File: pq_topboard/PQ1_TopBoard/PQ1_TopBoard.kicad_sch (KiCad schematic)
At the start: 11 parts, among them IC3 TCN75AVUA713, J2 Conn_01x11_MountingPin

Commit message: Functional revision and finishing touches part II
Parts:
- removed D8: SLCD-61N8, SOD-123_L2.8-W1.8-LS3.7-RD, symbol Top_board-altium-import:1_SLCD-61N8
- removed GA6, GA7, GA8: 5k, R0805, symbol Top_board-altium-import:1_5k
- removed R11, R12, VA6, VA7, VA8: 5k, R0805, symbol Top_board-altium-import:0_5k
- added Annotation1: Silkscreen_Annotation, symbols-nsl:IEEE_logo, symbol symbols-nsl:Silkscreen_Annotation
- added Annotation2: Silkscreen_Annotation, symbols-nsl:GRSS, symbol symbols-nsl:Silkscreen_Annotation
- added Annotation3: Silkscreen_Annotation, symbols-nsl:NSL_long, symbol symbols-nsl:Silkscreen_Annotation
- added Annotation4: Silkscreen_Annotation, symbols-nsl:Telecos, symbol symbols-nsl:Silkscreen_Annotation
- added Annotation5: Silkscreen_Annotation, symbols-nsl:UPC_positiu, symbol symbols-nsl:Silkscreen_Annotation
- added C1: 1 uF, Capacitor_SMD:C_0603_1608Metric, symbol Device:C
- added D1: SLCD-61N8, passive-nsl:SLCD-61N8, symbol passive-nsl:SLCD-61N8
- added GA0, GA1, GA2: 0R, Resistor_SMD:R_0805_2012Metric, symbol Lateral_board-altium-import:1_5k
- added H1, H2, H3, H4: MountingHole_Pad, MountingHole:MountingHole_3.2mm_M3_ISO14580_Pad, symbol Mechanical:MountingHole_Pad
- added H5: MountingHole, MountingHole:MountingHole_8.4mm_M8, symbol Mechanical:MountingHole
- added VA0, VA1, VA2: 0R, Resistor_SMD:R_0805_2012Metric, symbol Lateral_board-altium-import:0_5k
- J1: renamed from J2; footprint (none) -> Connector_Molex:Molex_PicoBlade_53261-0971_1x09-1MP_P1.25mm_Horizontal; symbol Connector_Generic_MountingPin:Conn_01x11_MountingPin -> Connector_Generic_MountingPin:Conn_01x09_MountingPin
- renumbered IC3 to IC1
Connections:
- net GND: now also J1.2 (Pin_2), J1.3 (Pin_3), J1.MP (MountPin), C1.2, GA0.1, GA1.1, GA2.1, H1.1, H2.1, H3.1, H4.1; no longer J1.11 (Pin_11)
- net VCC: now also C1.1, VA0.2, VA1.2, VA2.2; no longer J1.4 (Pin_4)
- net at IC1.7 (A0): now also GA0.2, VA0.1
- net at IC1.5 (A2): now also GA2.2, VA2.1
- net at IC1.6 (A1): now also GA1.2, VA1.1
- net BURNCOMMS: now reaches J1.9 (Pin_9)
- net SOLAR_Y: now reaches J1.1 (Pin_1)
- net PH-: now reaches J1.7 (Pin_7)
- net PH-: now also D1.1
- net PH+: now reaches J1.8 (Pin_8)
- net PH+: now also D1.2
- new net 3V3_PERM: J1.4 (Pin_4)
- no-connect marks 6 -> 0
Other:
- note added: "Lens Hole"
- note added: "Mounting holes"
- note added: "Photodiode"
- note added: "Picoblade connector"
- note added: "Temperature sensor"
- moved on the sheet: IC1

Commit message: Full Kicad7 transition, library improvement and adaptation, correct footprints and 3D models added
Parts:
- Annotation1: footprint symbols-nsl:IEEE_logo -> -nsl_symbols:IEEE_logo
- Annotation2: footprint symbols-nsl:GRSS -> -nsl_symbols:GRSS
- Annotation3: footprint symbols-nsl:NSL_long -> -nsl_symbols:NSL_long
- Annotation4: footprint symbols-nsl:Telecos -> -nsl_symbols:Telecos
- Annotation5: footprint symbols-nsl:UPC_positiu -> -nsl_symbols:UPC_positiu
- D1: footprint passive-nsl:SLCD-61N8 -> -nsl_passive:SLCD-61N8
- IC1: footprint Package_SO:SOP-8_3.9x4.9mm_P1.27mm -> -nsl_sensor:TCN75AVOA

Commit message: Small changes of component fields for the BOM
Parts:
- GA0, GA1, GA2, VA0, VA1, VA2: Manufacturer 1 (none) -> Vishay / Dale; Manufacturer Part Number 1 (none) -> CRCW08055K00JNTA; Supplier 1 (none) -> Mouser; Supplier Part Number 1 (none) -> 71-CRCW0805J-5K
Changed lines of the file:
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@@
       (effects (font (size 1.27 1.27)) (justify left bottom) hide)
+    )
+    (property "Manufacturer 1" "Vishay / Dale" (at 155.575 130.175 0)
+      (effects (font (size 1.27 1.27)) hide)
+    )
+    (property "Manufacturer Part Number 1" "CRCW08055K00JNTA" (at 155.575 130.175 0)
+      (effects (font (size 1.27 1.27)) hide)
+    )
+    (property "Supplier 1" "Mouser" (at 155.575 130.175 0)
+      (effects (font (size 1.27 1.27)) hide)
+    )
+    (property "Supplier Part Number 1" "71-CRCW0805J-5K" (at 155.575 130.175 0)
+      (effects (font (size 1.27 1.27)) hide)
     )
     (pin "1")
@@
       (effects (font (size 1.27 1.27)) (justify left bottom) hide)
     )
+    (property "Manufacturer 1" "Vishay / Dale" (at 177.165 120.015 0)
+      (effects (font (size 1.27 1.27)) hide)
+    )
+    (property "Manufacturer Part Number 1" "CRCW08055K00JNTA" (at 177.165 120.015 0)
+      (effects (font (size 1.27 1.27)) hide)
+    )
+    (property "Supplier 1" "Mouser" (at 177.165 120.015 0)
+      (effects (font (size 1.27 1.27)) hide)
+    )
+    (property "Supplier Part Number 1" "71-CRCW0805J-5K" (at 177.165 120.015 0)
+      (effects (font (size 1.27 1.27)) hide)
+    )
     (pin "1")
     (pin "2")
@@
       (effects (font (size 1.27 1.27)) (justify left bottom) hide)
     )
+    (property "Manufacturer 1" "Vishay / Dale" (at 177.165 109.855 0)
+      (effects (font (size 1.27 1.27)) hide)
+    )
+    (property "Manufacturer Part Number 1" "CRCW08055K00JNTA" (at 177.165 109.855 0)
+      (effects (font (size 1.27 1.27)) hide)
+    )
+    (property "Supplier 1" "Mouser" (at 177.165 109.855 0)
+      (effects (font (size 1.27 1.27)) hide)
+    )
+    (property "Supplier Part Number 1" "71-CRCW0805J-5K" (at 177.165 109.855 0)
+      (effects (font (size 1.27 1.27)) hide)
+    )
     (pin "1")
     (pin "2")
@@
     (property "BOM_LINK" "https://www.mouser.es/ProductDetail/Vishay-Dale/CRCW08055K00JNTA?qs=%2Fha2pyFadui6t5gBae62ocFJ46SNue422n5luvT1xmc7fnXInubqKA%3D%3D" (at 164.465 130.175 0)
       (effects (font (size 1.27 1.27)) (justify left bottom) hide)
+    )
+    (property "Manufacturer 1" "Vishay / Dale" (at 164.465 130.175 0)
+      (effects (font (size 1.27 1.27)) hide)
+    )
+    (property "Manufacturer Part Number 1" "CRCW08055K00JNTA" (at 164.465 130.175 0)
+      (effects (font (size 1.27 1.27)) hide)
+    )
+    (property "Supplier 1" "Mouser" (at 164.465 130.175 0)
+      (effects (font (size 1.27 1.27)) hide)
+    )
+    (property "Supplier Part Number 1" "71-CRCW0805J-5K" (at 164.465 130.175 0)
+      (effects (font (size 1.27 1.27)) hide)
     )
     (pin "1")
@@
     (property "BOM_LINK" "https://www.mouser.es/ProductDetail/Vishay-Dale/CRCW08055K00JNTA?qs=%2Fha2pyFadui6t5gBae62ocFJ46SNue422n5luvT1xmc7fnXInubqKA%3D%3D" (at 177.165 114.935 0)
       (effects (font (size 1.27 1.27)) (justify left bottom) hide)
+    )
+    (property "Manufacturer 1" "Vishay / Dale" (at 177.165 114.935 0)
+      (effects (font (size 1.27 1.27)) hide)
+    )
+    (property "Manufacturer Part Number 1" "CRCW08055K00JNTA" (at 177.165 114.935 0)
+      (effects (font (size 1.27 1.27)) hide)
+    )
+    (property "Supplier 1" "Mouser" (at 177.165 114.935 0)
+      (effects (font (size 1.27 1.27)) hide)
+    )
+    (property "Supplier Part Number 1" "71-CRCW0805J-5K" (at 177.165 114.935 0)
+      (effects (font (size 1.27 1.27)) hide)
     )
     (pin "1")
@@
       (effects (font (size 1.27 1.27)) (justify left bottom) hide)
     )
-    (pin "1")
+    (property "Manufacturer 1" "Vishay / Dale" (at 170.815 130.175 0)
+      (effects (font (size 1.27 1.27)) hide)
+    )
+    (property "Manufacturer Part Number 1" "CRCW08055K00JNTA" (at 170.815 130.175 0)
+      (effects (font (size 1.27 1.27)) hide)
+    )
+    (property "Supplier 1" "Mouser" (at 170.815 130.175 0)
+      (effects (font (size 1.27 1.27)) hide)
+    )
+    (property "Supplier Part Number 1" "71-CRCW0805J-5K" (at 170.815 130.175 0)
+      (effects (font (size 1.27 1.27)) hide)
+    )
+    (pin "1")

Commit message: BOM creation schematic changes 2.0
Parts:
- D1: Manufacturer 1 (none) -> Advanced Photonix; Manufacturer Part Number 1 (none) -> SLCD-61N8; Supplier 1 (none) -> Farnell; Supplier Part Number 1 (none) -> 1218991
- H1, H2, H3, H4, H5: Manufacturer 1 (none) -> N/A; Manufacturer Part Number 1 (none) -> N/A; Supplier 1 (none) -> N/A; Supplier Part Number 1 (none) -> N/A
- IC1: Manufacturer 1 (none) -> Microchip; Manufacturer Part Number 1 (none) -> TCN75AVOA; Supplier 1 (none) -> Mouser; Supplier Part Number 1 (none) -> 579-TCN75AVOA
- J1: Manufacturer 1 (none) -> MOLEX; Manufacturer Part Number 1 (none) -> Picoblade-53261-0971; Supplier 1 (none) -> Mouser; Supplier Part Number 1 (none) -> 538-53261-0971
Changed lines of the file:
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@@
+      (effects (font (size 1.27 1.27)) hide)
+    )
+    (property "Manufacturer 1" "N/A" (at 73.66 79.375 0)
+      (effects (font (size 1.27 1.27)) hide)
+    )
+    (property "Manufacturer Part Number 1" "N/A" (at 73.66 79.375 0)
+      (effects (font (size 1.27 1.27)) hide)
+    )
+    (property "Supplier 1" "N/A" (at 73.66 79.375 0)
+      (effects (font (size 1.27 1.27)) hide)
+    )
+    (property "Supplier Part Number 1" "N/A" (at 73.66 79.375 0)
       (effects (font (size 1.27 1.27)) hide)
     )
@@
     )
     (property "Datasheet" "~" (at 104.775 133.35 0)
+      (effects (font (size 1.27 1.27)) hide)
+    )
+    (property "Manufacturer 1" "N/A" (at 104.775 133.35 0)
+      (effects (font (size 1.27 1.27)) hide)
+    )
+    (property "Manufacturer Part Number 1" "N/A" (at 104.775 133.35 0)
+      (effects (font (size 1.27 1.27)) hide)
+    )
+    (property "Supplier 1" "N/A" (at 104.775 133.35 0)
+      (effects (font (size 1.27 1.27)) hide)
+    )
+    (property "Supplier Part Number 1" "N/A" (at 104.775 133.35 0)
       (effects (font (size 1.27 1.27)) hide)
     )
@@
       (effects (font (size 1.27 1.27)) hide)
     )
+    (property "Manufacturer 1" "N/A" (at 110.49 78.74 0)
+      (effects (font (size 1.27 1.27)) hide)
+    )
+    (property "Manufacturer Part Number 1" "N/A" (at 110.49 78.74 0)
+      (effects (font (size 1.27 1.27)) hide)
+    )
+    (property "Supplier 1" "N/A" (at 110.49 78.74 0)
+      (effects (font (size 1.27 1.27)) hide)
+    )
+    (property "Supplier Part Number 1" "N/A" (at 110.49 78.74 0)
+      (effects (font (size 1.27 1.27)) hide)
+    )
     (pin "1")
     (instances
@@
       (effects (font (size 1.27 1.27)) hide)
     )
+    (property "Manufacturer 1" "Advanced Photonix" (at 83.185 135.255 0)
+      (effects (font (size 1.27 1.27)) hide)
+    )
+    (property "Manufacturer Part Number 1" "SLCD-61N8" (at 83.185 135.255 0)
+      (effects (font (size 1.27 1.27)) hide)
+    )
+    (property "Supplier 1" "Farnell" (at 83.185 135.255 0)
+      (effects (font (size 1.27 1.27)) hide)
+    )
+    (property "Supplier Part Number 1" "1218991" (at 83.185 135.255 0)
+      (effects (font (size 1.27 1.27)) hide)
+    )
     (pin "1")
     (pin "2")
@@
       (effects (font (size 1.27 1.27)) hide)
     )
+    (property "Manufacturer 1" "N/A" (at 142.875 78.105 0)
+      (effects (font (size 1.27 1.27)) hide)
+    )
+    (property "Manufacturer Part Number 1" "N/A" (at 142.875 78.105 0)
+      (effects (font (size 1.27 1.27)) hide)
+    )
+    (property "Supplier 1" "N/A" (at 142.875 78.105 0)
+      (effects (font (size 1.27 1.27)) hide)
+    )
+    (property "Supplier Part Number 1" "N/A" (at 142.875 78.105 0)
+      (effects (font (size 1.27 1.27)) hide)
+    )
     (pin "1")
     (instances
@@
     )
     (property "Datasheet" "~" (at 173.355 78.105 0)
+      (effects (font (size 1.27 1.27)) hide)
+    )
+    (property "Manufacturer 1" "N/A" (at 173.355 78.105 0)
+      (effects (font (size 1.27 1.27)) hide)
+    )
+    (property "Manufacturer Part Number 1" "N/A" (at 173.355 78.105 0)
+      (effects (font (size 1.27 1.27)) hide)
+    )
+    (property "Supplier 1" "N/A" (at 173.355 78.105 0)
+      (effects (font (size 1.27 1.27)) hide)
+    )
+    (property "Supplier Part Number 1" "N/A" (at 173.355 78.105 0)
       (effects (font (size 1.27 1.27)) hide)
     )
@@
     )
     (property "Datasheet" "" (at 136.525 109.855 0)
+      (effects (font (size 1.27 1.27)) hide)
+    )
+    (property "Manufacturer 1" "Microchip" (at 136.525 109.855 0)
+      (effects (font (size 1.27 1.27)) hide)
+    )
+    (property "Manufacturer Part Number 1" "TCN75AVOA" (at 136.525 109.855 0)
+      (effects (font (size 1.27 1.27)) hide)
+    )
+    (property "Supplier 1" "Mouser" (at 136.525 109.855 0)
+      (effects (font (size 1.27 1.27)) hide)
+    )
+    (property "Supplier Part Number 1" " 579-TCN75AVOA" (at 136.525 109.855 0)
       (effects (font (size 1.27 1.27)) hide)
     )
@@
       (effects (font (size 1.27 1.27)) hide)
     )
+    (property "Manufacturer 1" "MOLEX" (at 97.155 113.03 0)
+      (effects (font (size 1.27 1.27)) hide)
+    )
+    (property "Manufacturer Part Number 1" "Picoblade-53261-0971 " (at 97.155 113.03 0)
+      (effects (font (size 1.27 1.27)) hide)
+    )
+    (property "Supplier 1" "Mouser" (at 97.155 113.03 0)
+      (effects (font (size 1.27 1.27)) hide)
+    )
+    (property "Supplier Part Number 1" "538-53261-0971 " (at 97.155 113.03 0)
+      (effects (font (size 1.27 1.27)) hide)
+    )

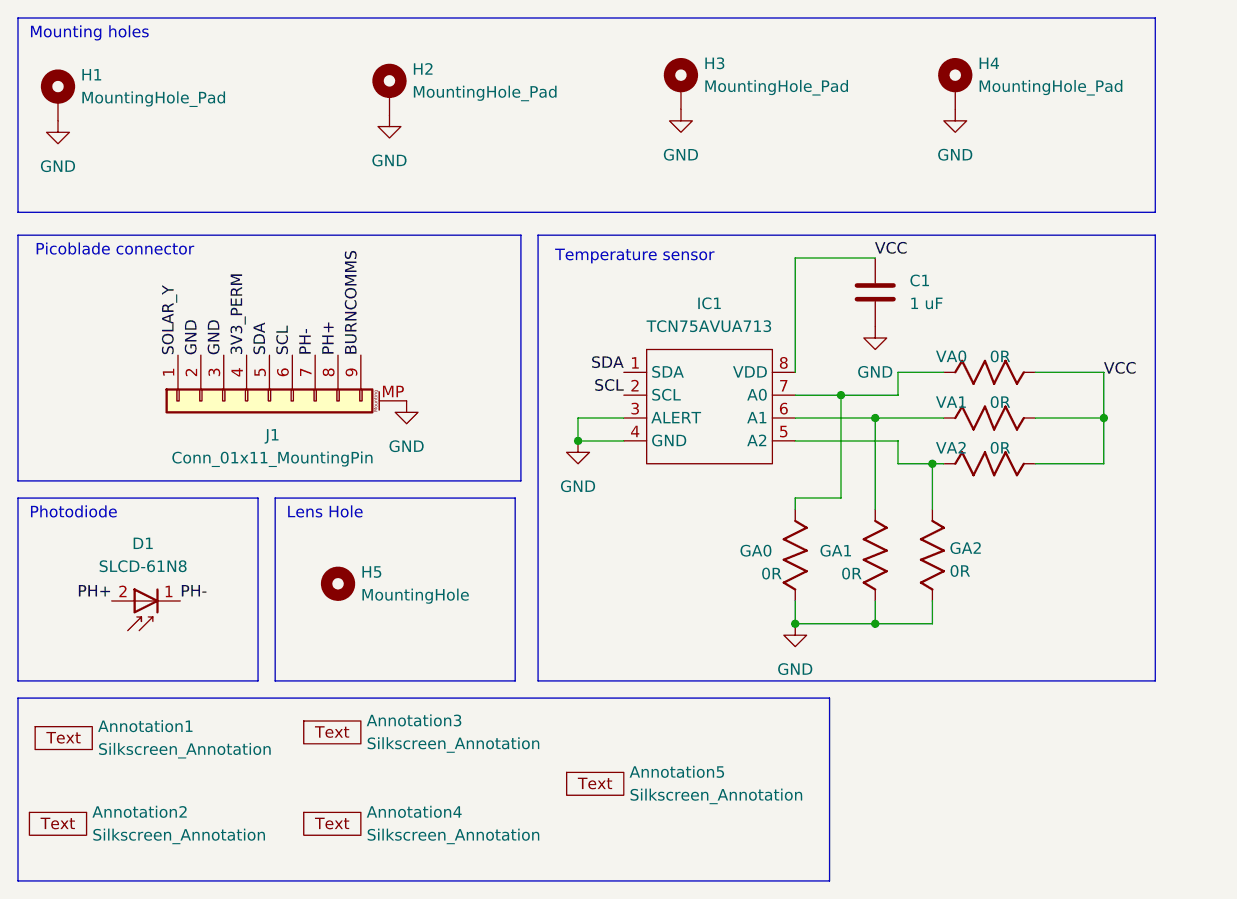
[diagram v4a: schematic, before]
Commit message: Added NSL lektron logo, reconciled library symbol - footprints, moved the picoblade connector so not to conflict with the top structure, fixed VCC trace issue
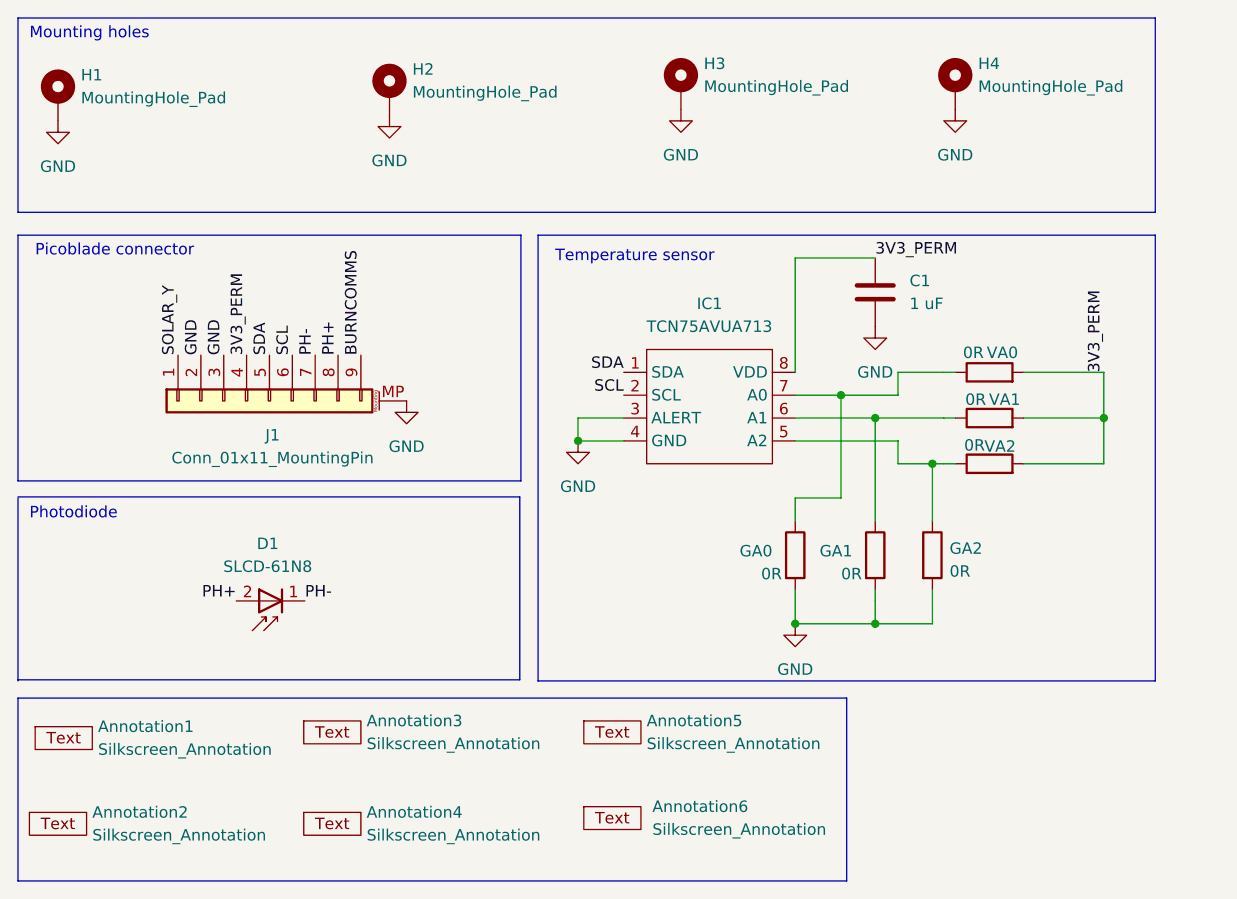
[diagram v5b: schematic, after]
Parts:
- removed H5: MountingHole, MountingHole:MountingHole_8.4mm_M8, symbol Mechanical:MountingHole
- added Annotation6: Silkscreen_Annotation, symbols-nsl:NSL_Lektron, symbol symbols-nsl:Silkscreen_Annotation
- Annotation1: footprint -nsl_symbols:IEEE_logo -> symbols-nsl:IEEE_logo
- Annotation2: footprint -nsl_symbols:GRSS -> symbols-nsl:GRSS
- Annotation3: footprint -nsl_symbols:NSL_long -> symbols-nsl:NSL_long
- Annotation4: footprint -nsl_symbols:Telecos -> symbols-nsl:Telecos
- Annotation5: footprint -nsl_symbols:UPC_positiu -> symbols-nsl:UPC_positiu
- D1: footprint -nsl_passive:SLCD-61N8 -> passive-nsl:SLCD-61N8
- GA0, GA1, GA2: symbol Lateral_board-altium-import:1_5k -> Device:R
- IC1: footprint -nsl_sensor:TCN75AVOA -> sensor-nsl:TCN75AVOA
- VA0, VA1, VA2: symbol Lateral_board-altium-import:0_5k -> Device:R
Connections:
- net VCC is gone; now on net 3V3_PERM: C1.1, IC1.8 (VDD), VA0.2, VA1.2, VA2.2
- net GND: now also GA0.2, GA1.2, GA2.2; no longer GA0.1, GA1.1, GA2.1
- net at IC1.7 (A0), VA0.1: now also GA0.1; no longer GA0.2
- net at IC1.5 (A2), VA2.1: now also GA2.1; no longer GA2.2
- net at IC1.6 (A1), VA1.1: now also GA1.1; no longer GA1.2
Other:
- note removed: "Lens Hole"
- moved on the sheet: Annotation5, D1
